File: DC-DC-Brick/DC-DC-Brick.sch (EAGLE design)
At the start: 20 parts

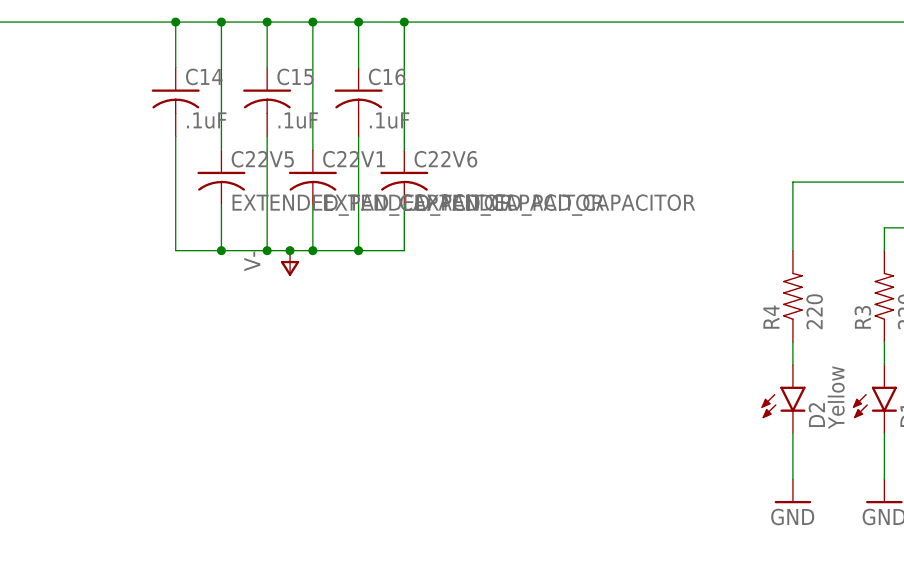
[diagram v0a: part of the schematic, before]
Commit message: FIxed connection issue
Gnd not connected in J purdue eye LED - fixed
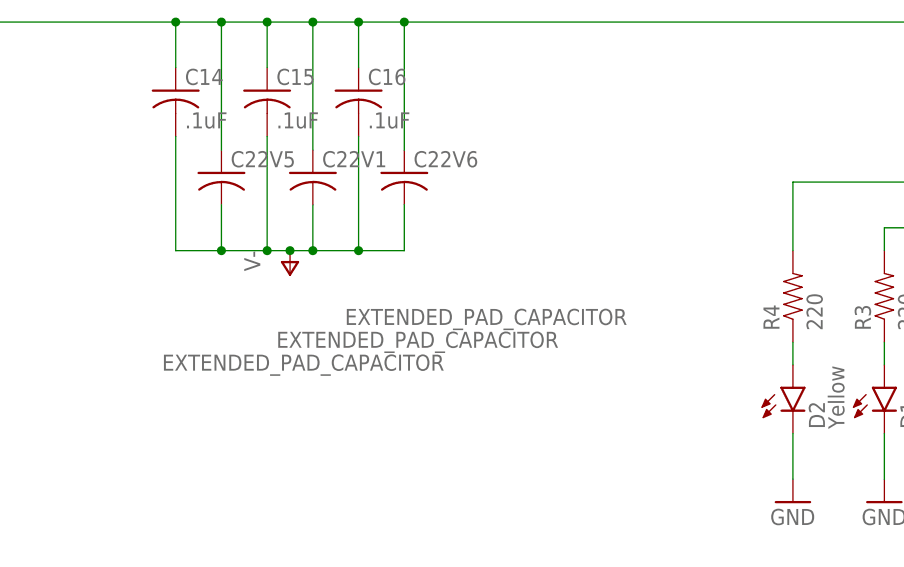
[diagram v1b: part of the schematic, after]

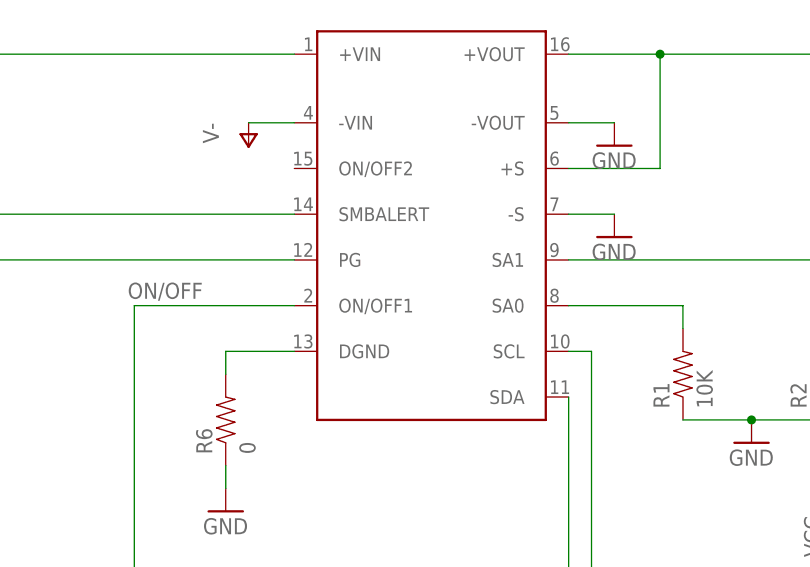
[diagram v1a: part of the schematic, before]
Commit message: Added debugging pins and more silk screen
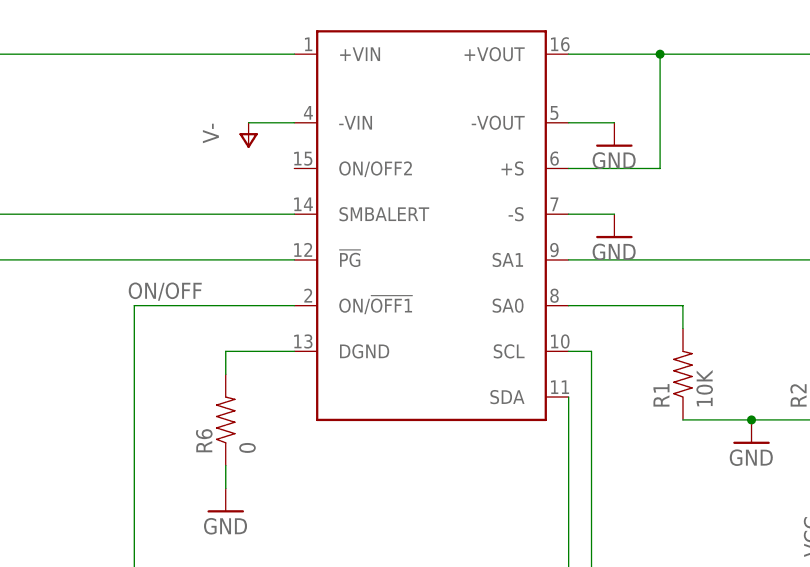
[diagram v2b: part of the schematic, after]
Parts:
- C22V1, C22V5, C22V6: device ExtendedPadCap:EXTENDED_PAD_CAPACITOR -> PowerComponents:EXTENDED_PAD_CAPACITOR
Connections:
- net N$7: now also U$1.!PG; no longer U$1.PG
- net ON/OFF: now also U$1.ON/!OFF1; no longer U$1.ON/OFF1
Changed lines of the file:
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@@
 <?xml version="1.0" encoding="utf-8"?>
 <!DOCTYPE eagle SYSTEM "eagle.dtd">
-<eagle version="7.6.0">
+<eagle version="7.7.0">
 <drawing>
 <settings>
@@
 <layer number="112" name="tSilk" color="7" fill="1" visible="yes" active="yes"/>
 <layer number="113" name="IDFDebug" color="4" fill="1" visible="yes" active="yes"/>
+<layer number="114" name="Badge_Outline" color="7" fill="1" visible="yes" active="yes"/>
+<layer number="115" name="ReferenceISLANDS" color="7" fill="1" visible="yes" active="yes"/>
 <layer number="116" name="Patch_BOT" color="9" fill="4" visible="yes" active="yes"/>
 <layer number="118" name="Rect_Pads" color="7" fill="1" visible="yes" active="yes"/>
@@
 <part name="C15" library="rcl" deviceset="C-US" device="C0603" value=".1uF"/>
 <part name="C16" library="rcl" deviceset="C-US" device="C0603" value=".1uF"/>
-<part name="C22V1" library="ExtendedPadCap" deviceset="EXTENDED_PAD_CAPACITOR" device=""/>
-<part name="C22V5" library="ExtendedPadCap" deviceset="EXTENDED_PAD_CAPACITOR" device=""/>
-<part name="C22V6" library="ExtendedPadCap" deviceset="EXTENDED_PAD_CAPACITOR" device=""/>
+<part name="C22V1" library="PowerComponents" deviceset="EXTENDED_PAD_CAPACITOR" device=""/>
+<part name="C22V5" library="PowerComponents" deviceset="EXTENDED_PAD_CAPACITOR" device=""/>
+<part name="C22V6" library="PowerComponents" deviceset="EXTENDED_PAD_CAPACITOR" device=""/>
 <part name="P-1" library="supply1" deviceset="V-" device=""/>
 <part name="GND5" library="supply1" deviceset="GND" device=""/>
@@
 <net name="N$7" class="0">
 <segment>
-<pinref part="U$1" gate="G$1" pin="PG"/>
+<pinref part="U$1" gate="G$1" pin="!PG"/>
 <wire x1="187.96" y1="139.7" x2="231.14" y2="139.7" width="0.1524" layer="91"/>
 <pinref part="R3" gate="G$1" pin="2"/>
@@
 <net name="ON/OFF" class="0">
 <segment>
-<pinref part="U$1" gate="G$1" pin="ON/OFF1"/>
+<pinref part="U$1" gate="G$1" pin="ON/!OFF1"/>
 <wire x1="231.14" y1="134.62" x2="213.36" y2="134.62" width="0.1524" layer="91"/>
 <wire x1="213.36" y1="134.62" x2="213.36" y2="91.44" width="0.1524" layer="91"/>
